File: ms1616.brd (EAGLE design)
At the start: 160 x 100 mm, 90 parts, among them IC101 ATMEGA32-PU, IC102 MAX483CPA, IC103 74594N, IC104 74594N, IC201 LTV847, IC202 LTV847, IC203 LTV847, IC204 LTV847, K301 S202S02, K302 S202S02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

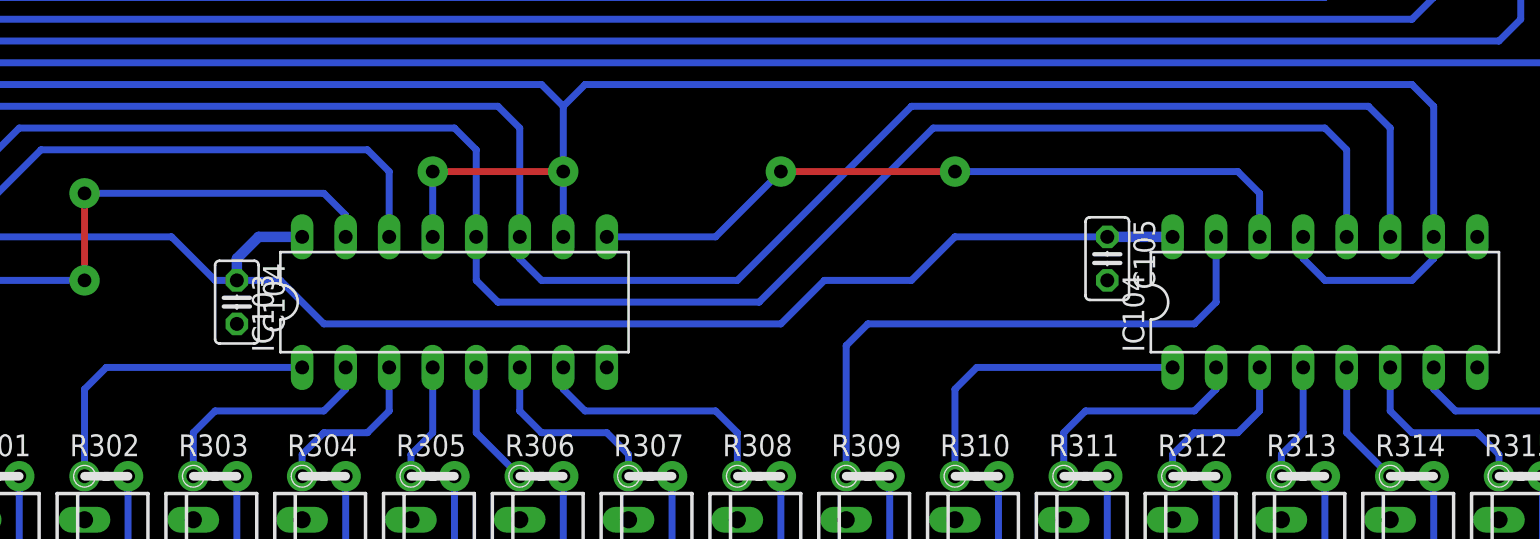
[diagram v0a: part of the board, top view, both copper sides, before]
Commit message: 74594 durch 74HC594 ersetzt
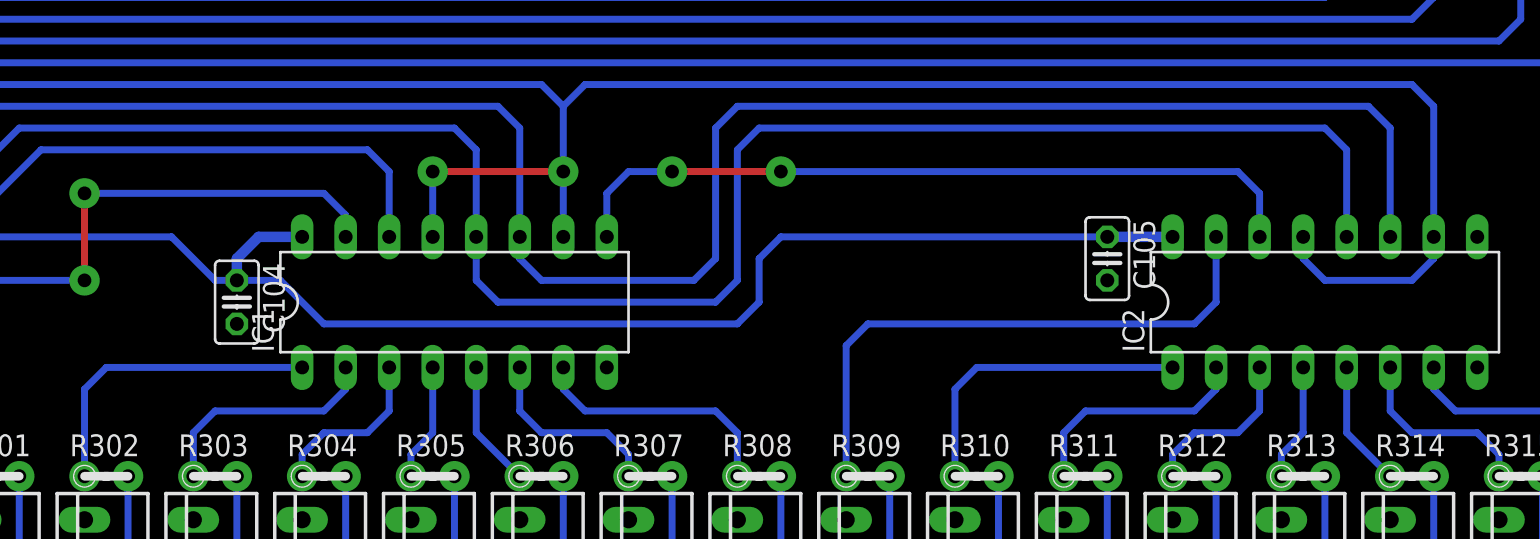
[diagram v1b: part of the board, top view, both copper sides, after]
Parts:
- removed IC103, IC104: 74594N, 74ttl-din:DIL16
- added IC1, IC2: 74HC594N, 74xx-eu:DIL16
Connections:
- net !R: now also IC1.10, IC1.13, IC2.10, IC2.13; no longer IC103.10, IC103.13, IC104.10, IC104.13
- net +5V: now also IC1.16, IC2.16; no longer IC103.16, IC104.16
- net C1: now also IC1.11, IC2.11; no longer IC103.11, IC104.11
- net C2: now also IC1.12, IC2.12; no longer IC103.12, IC104.12
- net D: now also IC1.14; no longer IC103.14
- net GND: now also IC1.8, IC2.8; no longer IC103.8, IC104.8
- net N$58: now also IC1.9, IC2.14; no longer IC103.9, IC104.14
- net OUT0: now also IC1.15; no longer IC103.15
- net OUT1: now also IC1.1; no longer IC103.1
- net OUT10: now also IC2.2; no longer IC104.2
- net OUT11: now also IC2.3; no longer IC104.3
- net OUT12: now also IC2.4; no longer IC104.4
- net OUT13: now also IC2.5; no longer IC104.5
- net OUT14: now also IC2.6; no longer IC104.6
- net OUT15: now also IC2.7; no longer IC104.7
- net OUT2: now also IC1.2; no longer IC103.2
- net OUT3: now also IC1.3; no longer IC103.3
- net OUT4: now also IC1.4; no longer IC103.4
- net OUT5: now also IC1.5; no longer IC103.5
- net OUT6: now also IC1.6; no longer IC103.6
- net OUT7: now also IC1.7; no longer IC103.7
- net OUT8: now also IC2.15; no longer IC104.15
- net OUT9: now also IC2.1; no longer IC104.1
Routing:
- net C2: track 147.6 -> 152.0 mm
- net C1: track 152.6 -> 157.1 mm
- net N$58: track 42.7 -> 44.2 mm
- net +5V: track 260.1 -> 261.6 mm

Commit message: Leichte korrekturen an Schematik und Layout
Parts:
- renumbered IC1 to IC103, IC2 to IC104
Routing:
- net N$63: track 36.5 -> 34.7 mm
- net +5V: track 261.6 -> 259.8 mm
- net N$61: track 41.6 -> 39.8 mm
- net N$64: track 39.0 -> 37.2 mm

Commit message: Echtzeituhr eingebaut
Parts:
- added C1: 10nF, passiv:C025-025X050
- added IC105: 74HC594N, 74xx-eu:DIL16
- added Q1: (no value), passiv:HC49/S
- IC102: value MAX483CPA -> DS1337; device ic-wandler:DIL08 -> ic-controller:DIL08
- IC103: value 74HC594N -> MAX483CPA; device 74xx-eu:DIL16 -> ic-wandler:DIL08
- S101: device schalter:DIP08YL -> schalter:DIP04YL
- moved IC102 65.4 mm to (17.8, 86.4), turned to 270 degrees
- moved IC103 54.3 mm to (33.0, 21.6), turned to 180 degrees
- moved IC104 50.8 mm to (83.8, 40.6)
- moved S101 9.16 mm to (17.8, 71.1), turned to 90 degrees
- moved C102 6.35 mm to (44.5, 61.0)
- moved C103 6.35 mm to (40.6, 19.1)
- moved IC101 6.35 mm to (33.0, 61.0)
- moved R101 6.35 mm to (16.5, 61.0)
- moved SV101 6.35 mm to (33.0, 94.0)
- moved V101 6.35 mm to (16.5, 21.6)
- moved X101 6.35 mm to (30.5, 5.08)
- moved C101 6.35 mm to (21.6, 61.0)
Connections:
- removed net N$128: IC101.3, S101.14
- removed net N$129: IC101.4, S101.13
- new net SCL: IC101.1, IC102.6
- new net SDA: IC101.2, IC102.5
- net !R: now also IC105.10, IC105.13; no longer IC103.10, IC103.13
- net +5V: now also C1.1, IC103.8, IC105.16; no longer IC103.16
- net C1: now also IC105.11; no longer IC103.11
- net C2: now also IC105.12; no longer IC103.12
- net D: now also IC104.14; no longer IC103.14
- net GND: now also C1.2, IC102.4, IC103.5, IC105.8; no longer IC102.5, IC103.8, S101.1, S101.2, S101.3, S101.4
- net N$122: now also S101.3; no longer S101.11
- net N$123: now also S101.2; no longer S101.10
- net N$124: now also IC103.7; no longer IC102.7
- net N$125: now also S101.1; no longer S101.9
- net N$126: now also IC102.1, Q1.2; no longer IC101.1, S101.16
- net N$127: now also IC102.2, Q1.1; no longer IC101.2, S101.15
- net N$130: now also S101.4; no longer S101.12
- net N$58: now also IC104.9, IC105.14; no longer IC103.9, IC104.14
- net N$61: now also IC103.4; no longer IC102.4
- net N$62: now also IC103.1; no longer IC102.1
- net N$63: now also IC103.2; no longer IC102.2
- net N$64: now also IC103.3; no longer IC102.3
- net N$74: now also IC103.6; no longer IC102.6
- net OUT0: now also IC104.15; no longer IC103.15
- net OUT1: now also IC104.1; no longer IC103.1
- net OUT10: now also IC105.2; no longer IC104.2
- net OUT11: now also IC105.3; no longer IC104.3
- net OUT12: now also IC105.4; no longer IC104.4
- net OUT13: now also IC105.5; no longer IC104.5
- net OUT14: now also IC105.6; no longer IC104.6
- net OUT15: now also IC105.7; no longer IC104.7
- net OUT2: now also IC104.2; no longer IC103.2
- net OUT3: now also IC104.3; no longer IC103.3
- net OUT4: now also IC104.4; no longer IC103.4
- net OUT5: now also IC104.5; no longer IC103.5
- net OUT6: now also IC104.6; no longer IC103.6
- net OUT7: now also IC104.7; no longer IC103.7
- net OUT8: now also IC105.15; no longer IC104.15
- net OUT9: now also IC105.1; no longer IC104.1
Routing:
- net C1: track 157.1 -> 150.7 mm
- net IN8: track 90.8 -> 84.4 mm
- net IN7: track 77.8 -> 71.4 mm
- net IN2: track 43.6 -> 37.2 mm
- net IN13: track 130.2 -> 123.9 mm
- net IN10: track 104.5 -> 98.2 mm
- net IN4: track 60.3 -> 54.0 mm
- net IN0: track 31.9 -> 25.6 mm
- net IN9: track 97.7 -> 91.3 mm
- net IN5: track 66.1 -> 59.8 mm
- net IN3: track 49.4 -> 43.1 mm
- net IN15: track 144.0 -> 137.6 mm
- net IN14: track 137.1 -> 130.8 mm
- net IN12: track 123.4 -> 117.0 mm
- net IN1: track 37.8 -> 31.4 mm
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
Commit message: Werte korrigiert
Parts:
- Q1: value (none) -> 32,768kHz
- R101: value (none) -> 10k
- V101: value TME2415S -> TME2405S
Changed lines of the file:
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@@
 <element name="R216" library="passiv" package="0204V" value="" x="148.59" y="87.63" rot="R270"/>
 <element name="SV101" library="stecker" package="ML6" value="" x="33.02" y="93.98"/>
-<element name="R101" library="passiv" package="0204V" value="" x="16.51" y="60.96" rot="R270"/>
+<element name="R101" library="passiv" package="0204V" value="10k" x="16.51" y="60.96" rot="R270"/>
 <element name="IC103" library="ic-wandler" package="DIL08" value="MAX483CPA" x="33.02" y="21.59" rot="R180"/>
-<element name="V101" library="schaltregler" package="TME-24V" value="TME2415S" x="16.51" y="21.59" rot="R90">
-<attribute name="OC_NEWARK" value="51R5332" x="16.51" y="21.59" size="1.778" layer="27" rot="R90" display="off"/>
-<attribute name="MPN" value="TME 2415S" x="16.51" y="21.59" size="1.778" layer="27" rot="R90" display="off"/>
+<element name="V101" library="schaltregler" package="TME-24V" value="TME2405S" x="16.51" y="21.59" rot="R90">
+<attribute name="OC_NEWARK" value="51R5329" x="16.51" y="21.59" size="1.778" layer="27" rot="R90" display="off"/>
+<attribute name="MPN" value="TME 2405S" x="16.51" y="21.59" size="1.778" layer="27" rot="R90" display="off"/>
 <attribute name="MF" value="" x="16.51" y="21.59" size="1.778" layer="27" rot="R90" display="off"/>
-<attribute name="OC_FARNELL" value="1007550" x="16.51" y="21.59" size="1.778" layer="27" rot="R90" display="off"/>
+<attribute name="OC_FARNELL" value="1007547" x="16.51" y="21.59" size="1.778" layer="27" rot="R90" display="off"/>
 </element>
 <element name="K309" library="relais" package="SIP4" value="S202S02" x="106.68" y="20.32" rot="R90">
@@
 </element>
 <element name="IC102" library="ic-controller" package="DIL08" value="DS1337" x="17.78" y="86.36" rot="R270"/>
-<element name="Q1" library="passiv" package="HC49/S" value="" x="7.62" y="86.36" rot="R90"/>
+<element name="Q1" library="passiv" package="HC49/S" value="32,768kHz" x="7.62" y="86.36" rot="R90"/>
 <element name="C1" library="passiv" package="C025-025X050" value="10nF" x="17.78" y="93.98" rot="R180"/>
 </elements>
@@
 </signal>
 </signals>
+<errors>
+</errors>
 </board>
 </drawing>
